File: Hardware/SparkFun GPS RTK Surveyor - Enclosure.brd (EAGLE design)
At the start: 69.1 x 111.1 mm, 96 parts

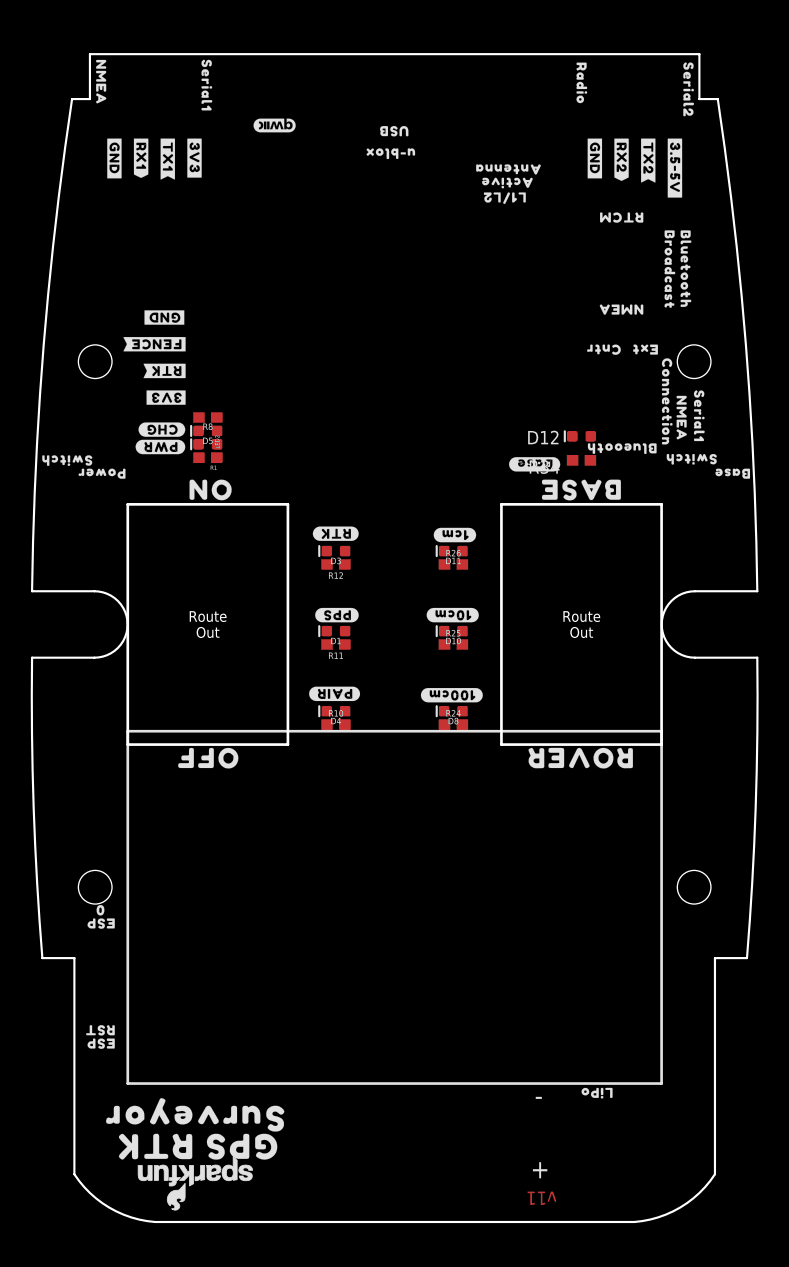
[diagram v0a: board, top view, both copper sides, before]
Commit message: v13 hardware. Fix power LED. Add gcode for enclosure.
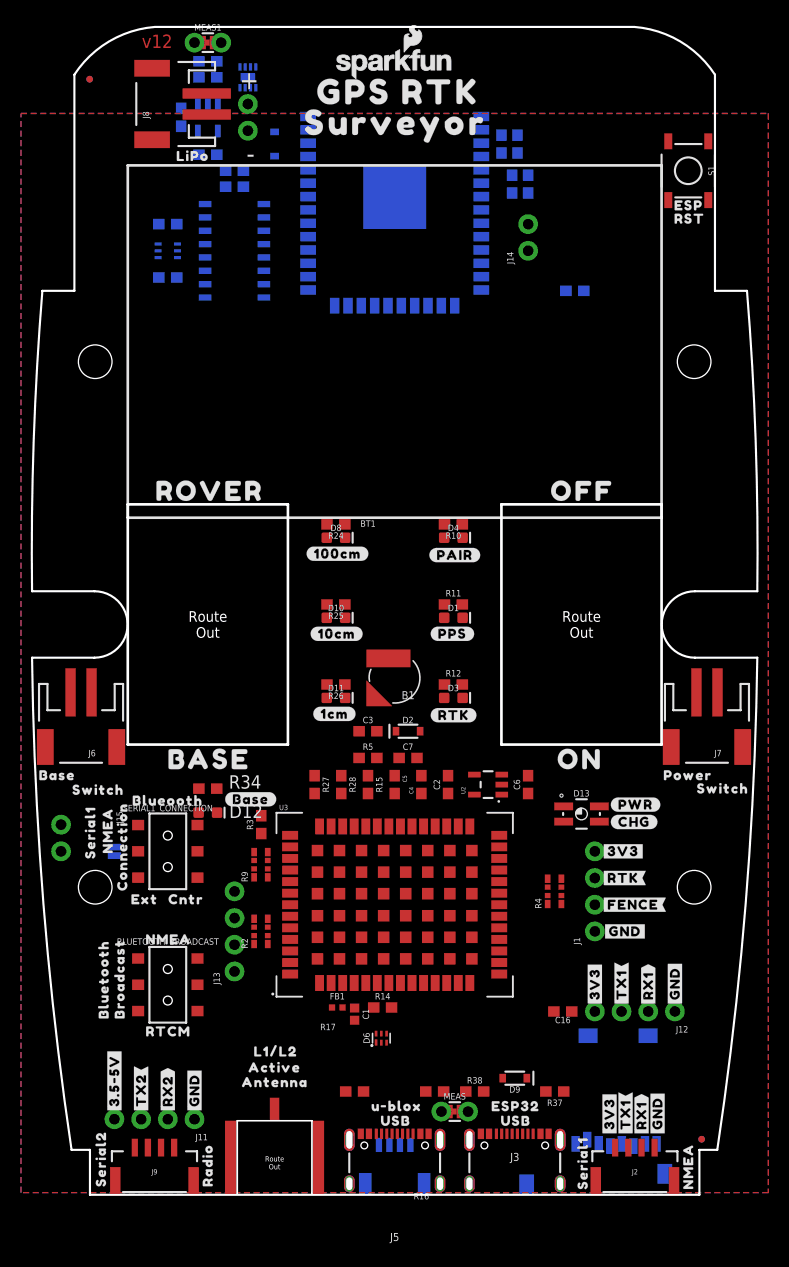
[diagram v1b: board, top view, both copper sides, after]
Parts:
- removed D5: Yellow, SparkFun-LED:LED-0603
- removed LED2: RED, SparkFun-LED:LED-0603
- removed R1, R8: 330, SparkFun-Resistors:0603
- added B1: 6.8MM_COIN_CELL, SparkFun-Batteries:ML414H_IV01E
- added BLUETOOTH_BROADCAST, SERIAL1_CONNECTION: (no value), SparkFun-Switches:SWITCH_DPDT_SMD_AYZ0202
- added BT1: LIPO-OUTLINE1100, SparkFun-Batteries:LIPO-1000
- added C1: 47pF, SparkFun-Capacitors:0402
- added C10, C14: 10uF, SparkFun-Capacitors:0603
- added C11, C12, C13, C15, C16, C5, C7: 0.1uF, SparkFun-Capacitors:0603
- added C2, C3, C4, C6: 1.0uF, SparkFun-Capacitors:0603
- added C8, C9: 4.7uF, SparkFun-Capacitors:0603
- added D13: RGB, SparkFun-LED:P-LCC-4-3
- added D2: 0.5A/40V/420mV, SparkFun-DiscreteSemi:SOD-323
- added D6: PRTR5V0U2F, SparkFun-IC-Power:SOT886
- added D7, D9: 3A/10V/280mV, SparkFun-DiscreteSemi:SOD-323
- added DUAL_OUTPUT: (no value), SparkFun-Jumpers:SMT-JUMPER_2_NO_SILK
- added E1: SMA, SparkFun-RF:SMA-EDGE-SMD
- added FB1: 2.66Ω, SparkFun-Coils:0402-TIGHT
- added J1, J11, J12, J13: (no value), SparkFun-Connectors:1X04_NO_SILK
- added J10, J14, J15: (no value), SparkFun-Connectors:1X02_NO_SILK
- added J16: microSD, SparkFun-Connectors:MICRO-SD-SOCKET
- added J2, J9: (no value), SparkFun-Connectors:JST-4-SMD-1.25MM-LOCKING
- added J3: USB-C, SparkFun-Connectors:USB-C-16P-2LAYER-PADS
- added J4: Qwiic Right Angle, SparkFun-Connectors:JST04_1MM_RA
- added J5: (no value), SparkFun-Connectors:USB-C-16P-2LAYER-PADS
- added J6: Start Base, SparkFun-Connectors:JST-2-SMD
- added J7: Power Switch, SparkFun-Connectors:JST-2-SMD
- added J8: (no value), SparkFun-Connectors:JST-2-SMD
- added JP21, JP61, JP71, JP81: FIDUCIALUFIDUCIAL, SparkFun-Aesthetics:FIDUCIAL-MICRO
- added LOGO1: OSHW-LOGOMINI, SparkFun-Aesthetics:OSHW-LOGO-MINI
- added LOGO2: SFE_LOGO_NAME_FLAME.1_INCH, SparkFun-Aesthetics:SFE_LOGO_NAME_FLAME_.1
- added MEAS, MEAS1: (no value), SparkFun-Jumpers:COMBO-JUMPER_2_NC_TRACE
- added Q2: MBT3904DW1T1, SparkFun-DiscreteSemi:SC70-6
- added R13, R15: 100k, SparkFun-Resistors:0603
- added R14: 10, SparkFun-Resistors:0603
- added R16, R17, R37, R38: 5.1k, SparkFun-Resistors:0603
- added R2, R4, R9: 33, SparkFun-Resistors:1206_RA
- added R20, R23, R29: 10k, SparkFun-Resistors:0603
- added R27, R28: 27, SparkFun-Resistors:0603
- added R3: 33, SparkFun-Resistors:0603
- added R5: 3.3k, SparkFun-Resistors:0603
- added R7: 1k, SparkFun-Resistors:0603
- added S1: RESET, SparkFun-Switches:TACTILE_SWITCH_SMD_5.2MM
- added U$66: (no value), output:USB1
- added U$67: (no value), output:ESP320
- added U$68: (no value), output:#RX1#2
- added U$82: (no value), output:#GND#0
- added U$83: (no value), output:MICROSD0
- added U1: MCP73831, SparkFun-IC-Power:SOT23-5
- added U2: 3.3V, SparkFun-IC-Power:SOT23-5
- added U3: U-BLOX_ZED-F9P, SparkFun-GPS:ZED-F9P
- added U5: ESP-WROOM-32NARROW, SparkFun-RF:ESP-WROOM-32-NARROW
- added U6: CH340C, SparkFun-IC-Comms:SO016
- added U7: MAX17048, SparkFun-IC-Power:DFN-8
- U$5: device output:ESP0 -> output:#3V3#0
- U$65: device output:02 -> output:#TX1#1
- moved U$49 122.4 mm to (27.9, -54.5), turned to 90 degrees
- moved U$43 122.0 mm to (-27.9, -54.2), turned to 90 degrees
- moved U$29 114.6 mm to (17.9, -54.5), turned to 90 degrees
- moved U$50 114.1 mm to (-17.8, -54.2), turned to 90 degrees
- moved U$48 108.5 mm to (25.0, -48.8), turned to 90 degrees
- moved U$23 107.3 mm to (-26.7, -46.6), turned to 90 degrees
- moved LOGO3 107.1 mm to (0.00, 53.3), turned to 0 degrees
- moved U$45 106.6 mm to (23.5, -48.8), turned to 90 degrees
- moved U$40 104.9 mm to (-24.1, -46.6), turned to 90 degrees
- moved U$46 104.8 mm to (22.0, -48.8), turned to 90 degrees
- moved U$47 103.2 mm to (20.4, -48.8), turned to 90 degrees
- moved U$39 102.7 mm to (-21.6, -46.6), turned to 90 degrees
- moved U$38 100.6 mm to (-19.1, -46.6), turned to 90 degrees
- moved U$70 100.3 mm to (-9.14, 50.7), turned to 0 degrees
- moved U$27 98.9 mm to (-21.5, 44.6), turned to 0 degrees
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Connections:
- removed net ESP32_12/BLUETOOTH_STATUS: R10.1
- removed net ESP32_13/POSACC3: R24.1
- removed net ESP32_15/POSACC2: R25.1
- removed net ESP32_2/POSACC1: R26.1
- removed net ESP32_4/BASE_STAT: R34.1
- removed net N$10: LED2.A, R1.1
- removed net N$8: D5.C, R8.2
- removed net PPS_STAT: R11.2
- removed net RTK_STAT: D3.C
- new net 5V: C6.1, J11.4, J7.1, J9.1, U2.1, U2.3
- new net ANT_VCC: C1.1, FB1.2, R14.1
- new net BACKUP: B1.+, C3.1, R5.1, U3.36
- new net CC1: J5.A5, R17.2
- new net CC2: J5.B5, R16.2
- new net CC3: J3.B5, R37.2
- new net CC4: J3.A5, R38.2
- new net D+: D6.4, R27.1
- new net D+1: J3.A6, J3.B6, U6.5
- new net D-: D6.6, R28.1
- new net D-1: J3.A7, J3.B7, U6.6
- new net ESP32_!DTR: Q2.1, R23.1, U6.13
- new net ESP32_!RTS: Q2.4, R29.1, U6.14
- new net ESP32_EN: C12.1, Q2.3, R20.1, S1.3, S1.4, U5.3
- new net ESP32_RXI: U5.34, U6.2
- new net ESP32_TXO: U5.35, U6.3
- new net ESP_0/BOOT: Q2.6, U5.25
- new net ESP_12/LED_BLUETOOTH: R10.1, U5.14
- new net ESP_13/LED_100CM: R24.1, U5.16
- new net ESP_14: U5.13
- new net ESP_15/LED_10CM: R25.1, U5.23
- new net ESP_16/BT_RXI: BLUETOOTH_BROADCAST.5, U5.27
- new net ESP_17/BT_TXO: BLUETOOTH_BROADCAST.2, U5.28
- new net ESP_18/SD_SCK: J16.SCLK, U5.30
- new net ESP_19/SD_CIPO: J16.DO/DAT0, U5.31
- new net ESP_2/LED_1CM: R26.1, U5.24
- new net ESP_21/SDA: J4.3, R9.P6, U5.33, U7.8
- new net ESP_22/SCL: J4.4, R9.P7, U5.36, U7.7
- new net ESP_23/SD_COPI: J16.DI/CMD, U5.37
- new net ESP_25/SD_!CS!: J16.CS/DAT3, R13.1, U5.10
- new net ESP_26/ZED_TX_READY: J13.4, R9.P8, U5.11
- new net ESP_27/ZED_!RESET!: J13.3, R2.P5, U5.12
- new net ESP_32: J14.2, U5.8
- new net ESP_33: J14.1, U5.9
- new net ESP_34/PWR_LVL_RED: D13.1, U5.6
- new net ESP_35/PWR_LVL_GRN: D13.2, U5.7
- new net ESP_36/BATT_ALRT: U5.4, U7.5
- new net ESP_4/LED_BASE_STAT: R34.1, U5.26
- new net ESP_5/SWITCH_BASE_SELECT: J6.1, U5.29
- new net ESP_I39: U5.5
- new net EXTERNAL_SERIAL1_RXI: J12.2, J2.3, SERIAL1_CONNECTION.3
- new net EXTERNAL_SERIAL1_TXO: DUAL_OUTPUT.2, J12.3, J2.2, SERIAL1_CONNECTION.6
- new net FENCE_LV: R4.P8, U3.19
- new net GPS_ANT1: E1.SIG, FB1.1, U3.2
- new net N$11: R27.2, U3.40
- new net N$12: R28.2, U3.39
- new net N$13: R14.2, U3.7
- new net N$16: R2.P4, U3.49
- new net N$18: R2.P3, U3.50
- new net N$22: R9.P1, U3.46
- new net N$24: Q2.5, R23.2
- new net N$25: Q2.2, R29.2
- new net N$32: D9.A, J3.VBUS1, J3.VBUS2
- new net N$4: J5.VBUS1, J5.VBUS2, MEAS.1, MEAS.3
- new net N$5: R7.2, U1.5
- new net N$6: D2.C, R5.2
- new net N$7: J8.2, MEAS1.1, MEAS1.3
- new net NMEA-RX: BLUETOOTH_BROADCAST.1, SERIAL1_CONNECTION.1
- new net NMEA-TX: BLUETOOTH_BROADCAST.4, DUAL_OUTPUT.1, SERIAL1_CONNECTION.4
- new net PPS: R2.P1, U3.53
- new net RTK_LV: R4.P7, U3.20
- new net RX2_LV: R4.P6, U3.26
- new net RXLV: R9.P4, U3.43
- new net SCL_LV: R9.P2, U3.45
- new net SDA_LV: R9.P3, U3.44
- new net TX2_LV: R4.P5, U3.27
- new net TXLV: R3.1, U3.42
- new net UNP_D+: D6.3, J5.A6, J5.B6
- new net UNP_D-: D6.1, J5.A7, J5.B7
- new net V_BATT: C15.1, C8.1, D7.A, J10.1, MEAS1.2, MEAS1.4, U1.3, U7.2, U7.3
- new net ZED-RXI1: J15.2, R9.P5, SERIAL1_CONNECTION.2
- new net ZED-RXI2: BLUETOOTH_BROADCAST.3, J11.2, J9.3, R4.P3
- new net ZED-TXO1: J15.1, R3.2, SERIAL1_CONNECTION.5
- new net ZED-TXO2: BLUETOOTH_BROADCAST.6, J11.3, J9.2, R4.P4
- new net ZED_!SAFE!: J13.2, R2.P6
- new net ZED_FENCE_STAT: J1.2, R4.P1
- new net ZED_PPS_STAT: J13.1, R11.2, R2.P8
- new net ZED_RTK_STAT: D3.C, J1.3, R4.P2
- net 3.3V: now also C10.1, C11.1, C13.1, C14.1, C16.1, C2.1, C4.1, C5.2, C7.2, D2.A, J1.4, J12.4, J16.VCC, J2.1, J4.2, R13.2, R15.2, R20.2, U2.5, U3.33, U3.34, U3.38, U5.2, U6.16, U6.4; no longer R1.2
- net CHG_LED: now also D13.3, U1.1; no longer R8.1
- net GND: now also B1.-, C1.2, C10.2, C11.2, C12.2, C13.2, C14.2, C15.2, C16.2, C2.2, C3.2, C4.2, C5.1, C6.2, C7.1, C8.2, C9.2, D6.2, E1.GND@0, E1.GND@1, J1.1, J10.2, J11.1, J12.1, J16.CD1, J16.GND, J16.GND1, J16.GND3, J2.4, J3.GND, J3.GND2, J3.SHLD1, J3.SHLD2, J3.SHLD3, J3.SHLD4, J4.1, J5.GND, J5.GND2, J5.SHLD1, J5.SHLD2, J5.SHLD3, J5.SHLD4, J6.2, J8.1, J9.4, R15.1, R16.1, R17.1, R37.1, R38.1, R7.1, S1.1, S1.2, U1.2, U2.2, U3.1, U3.100, U3.101, U3.102, U3.12, U3.14, U3.3, U3.32, U3.37, U3.41, U3.48, U3.55, U3.56, U3.57, U3.58, U3.59, U3.60, U3.61, U3.62, U3.63, U3.64, U3.65, U3.66, U3.67, U3.68, U3.69, U3.70, U3.71, U3.72, U3.73, U3.74, U3.75, U3.76, U3.77, U3.78, U3.79, U3.80, U3.81, U3.82, U3.83, U3.84, U3.85, U3.86, U3.87, U3.88, U3.89, U3.90, U3.91, U3.92, U3.93, U3.94, U3.95, U3.96, U3.97, U3.98, U3.99, U5.1, U5.15, U5.38, U5.GND, U6.1, U7.1, U7.4, U7.6, U7.9; no longer LED2.C
- net VIN: now also C9.1, D13.4, D6.5, D7.C, D9.C, J7.2, MEAS.2, MEAS.4, U1.4; no longer D5.A
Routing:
- added copper zone on layer 1, net GND
- added copper zone on layer 16, net GND
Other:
- outline, holes or cut-outs redrawn
- board text added: "v12"
- board text removed: "Measurements in inches"
- board text removed: "v11"
